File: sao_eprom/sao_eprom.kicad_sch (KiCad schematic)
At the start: 7 parts, among them U1 27C512, U2 24LC32

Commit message: Does more designing ROMulator
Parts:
- removed U1: 27C512, Package_DIP:DIP-28_W15.24mm, symbol Memory_EPROM:27C512
- removed U?: PCAL6416APW, Package_SO:TSSOP-24_4.4x7.8mm_P0.65mm, symbol Interface_Expansion:PCAL6416APW
- removed U? (x2): 74HC273, symbol 74xx:74HC273
- U5: renamed from U2; footprint (none) -> Package_SO:SOIC-8_3.9x4.9mm_P1.27mm
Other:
- added sheet EPROM interface (eprom.kicad_sch)
- note removed: "Address buffer"
- note removed: "EPROM socket"
- note removed: "I/O expander"
- moved on the sheet: JP1, SAO, U5

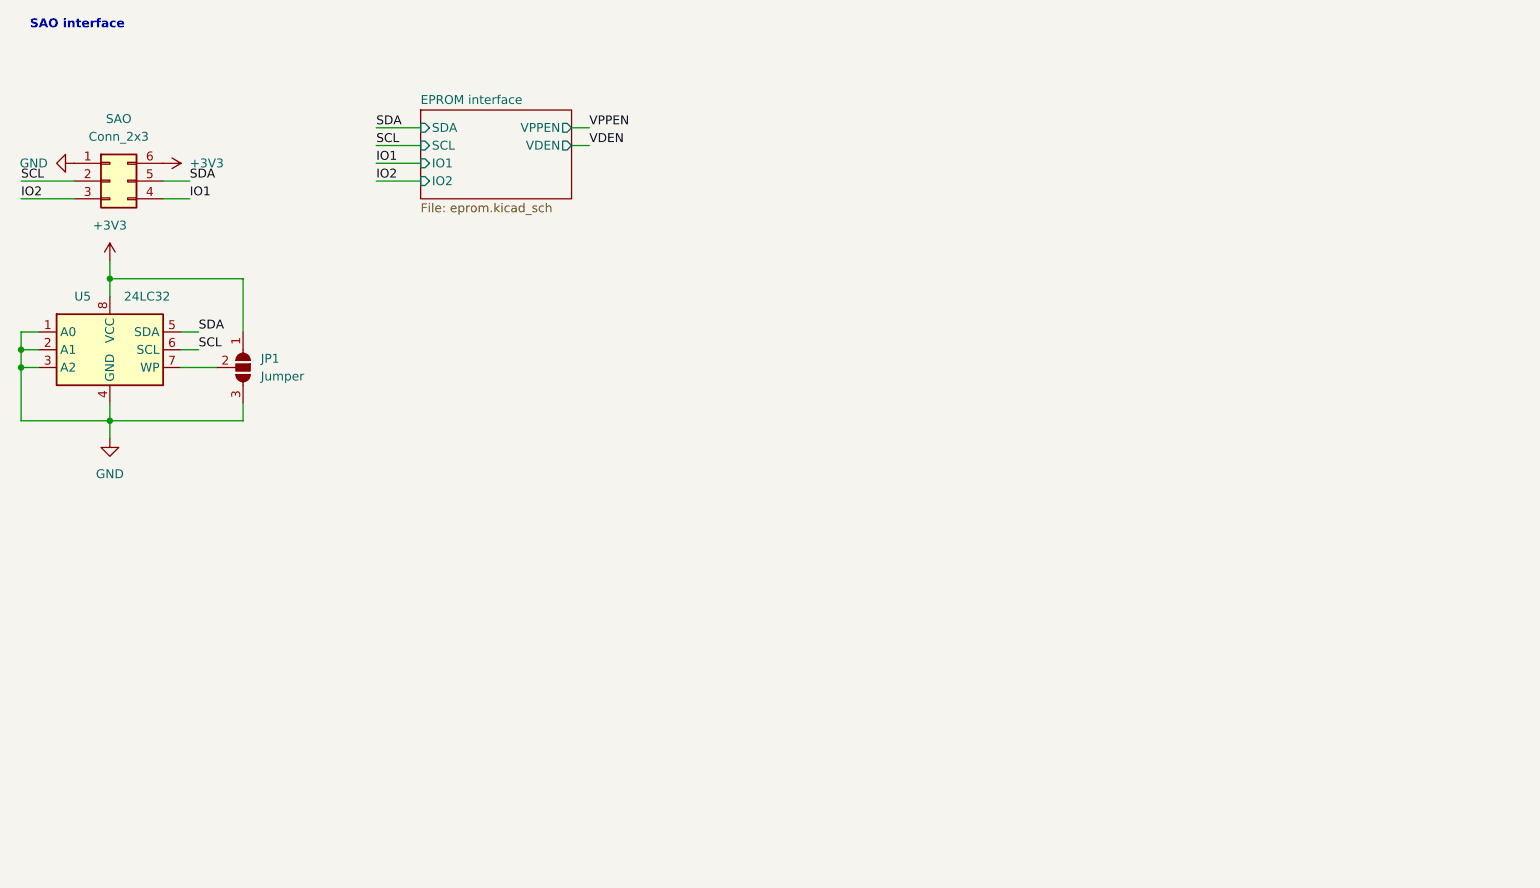
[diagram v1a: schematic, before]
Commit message: Reworks the address circuit
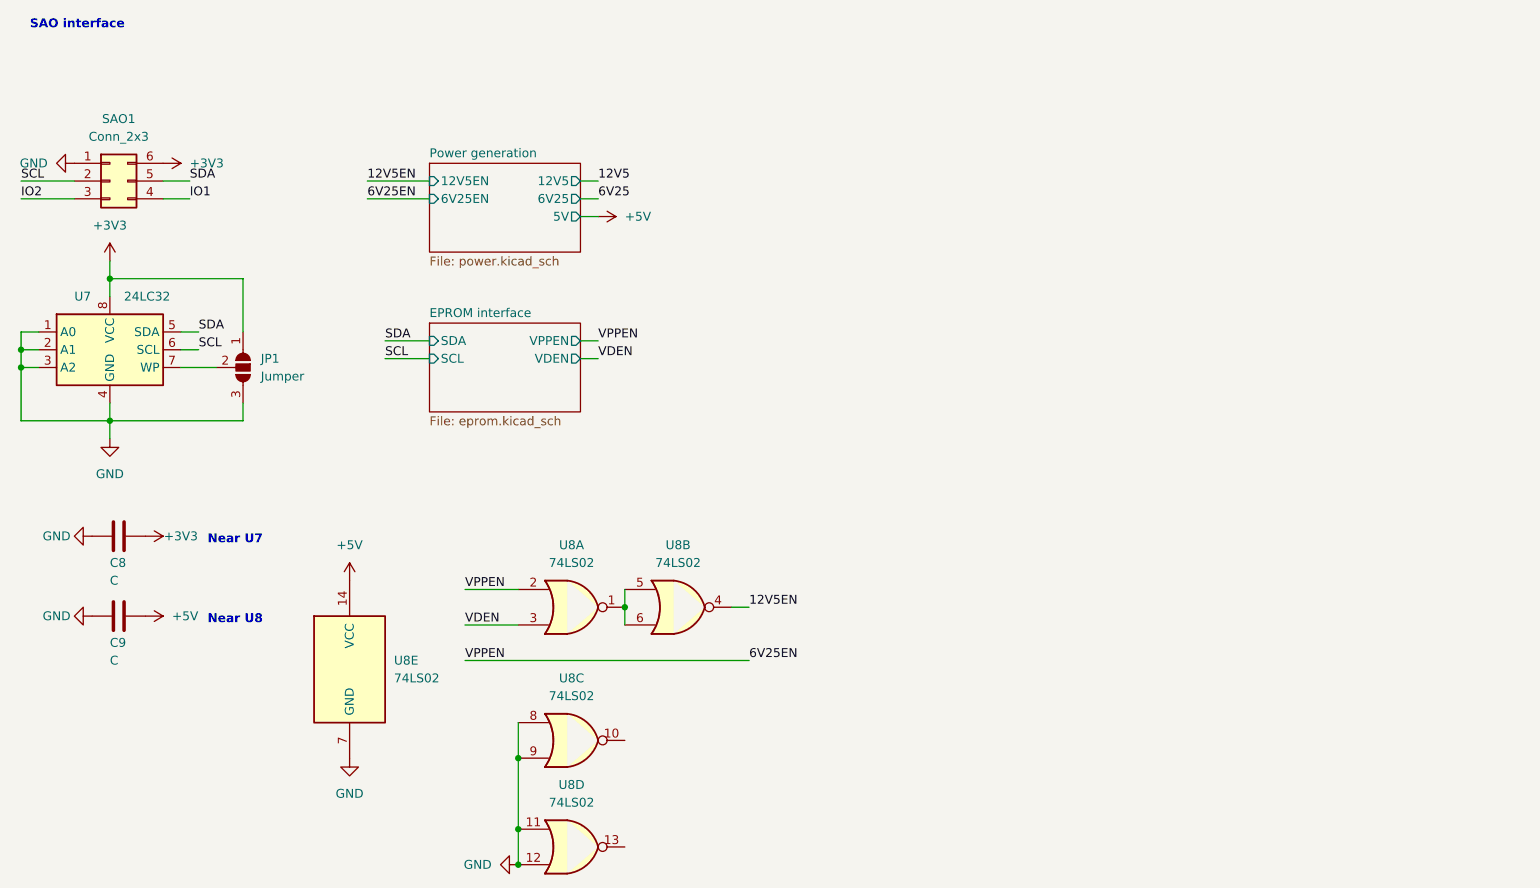
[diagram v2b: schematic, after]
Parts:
- added C8, C9: C, Capacitor_THT:C_Disc_D3.0mm_W1.6mm_P2.50mm, symbol Device:C
- added U8: 74LS02, Package_DIP:DIP-14_W7.62mm, symbol 74xx:74LS02
- JP1: footprint (none) -> Jumper:SolderJumper-3_P1.3mm_Open_RoundedPad1.0x1.5mm_NumberLabels
- SAO1: renamed from SAO; footprint (none) -> Connector_PinHeader_2.54mm:PinHeader_2x03_P2.54mm_Vertical
- renumbered U5 to U7
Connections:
- net +3V3: now also C8.1
- net GND: now also C8.2, C9.2, U8.11, U8.12, U8.7 (GND), U8.8, U8.9
- net VDEN: now also U8.3
- new net: U8.1, U8.5, U8.6
- new net +5V: C9.1, U8.14 (VCC)
- new net 12V5EN: U8.4
- new net 6V25EN: U8.2
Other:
- added sheet Power generation (power.kicad_sch)
- sheet EPROM interface ports: added none; removed IO1, IO2
- note added: "Near U7"
- note added: "Near U8"

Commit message: I know how 2 power now
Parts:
- removed C9: C, Capacitor_THT:C_Disc_D3.0mm_W1.6mm_P2.50mm, symbol Device:C
- removed U8: 74LS02, Package_DIP:DIP-14_W7.62mm, symbol 74xx:74LS02
- added Q1, Q3, Q5: RE1C002UNTCL, Package_TO_SOT_SMD:SOT-416, symbol Transistor_FET:2N7002E
- added Q2, Q4, Q6, Q7: RE1C002ZPTL, Package_TO_SOT_SMD:SOT-416, symbol Transistor_FET:AO3401A
- added R10, R12, R14, R16: 100R, Resistor_THT:R_Axial_DIN0207_L6.3mm_D2.5mm_P7.62mm_Horizontal, symbol Device:R
- added R11, R13, R15: 1K, Resistor_THT:R_Axial_DIN0207_L6.3mm_D2.5mm_P7.62mm_Horizontal, symbol Device:R
- added R17, R18: 10K, Resistor_THT:R_Axial_DIN0207_L6.3mm_D2.5mm_P7.62mm_Horizontal, symbol Device:R
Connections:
- net +5V: now also Q7.2 (S)
- net 12V5: now also Q2.2 (S), Q4.2 (S), R11.1, R13.1
- net 6V25: now also Q6.2 (S), R15.1
- net GND: now also Q1.2 (S), Q3.2 (S), Q5.2 (S), R17.1, R18.2
- net VDEN: now also R12.1, R18.1
- new net: Q1.1 (G), R10.2
- new net: Q1.3 (D), Q2.1 (G), R11.2
- new net: Q5.1 (G), R14.2
- new net: Q5.3 (D), Q6.1 (G), R15.2
- new net: Q7.1 (G), R16.2
- new net: Q3.1 (G), R12.2
- new net: Q3.3 (D), Q4.1 (G), R13.2
- new net VD: Q4.3 (D)
- new net VMEM: Q6.3 (D), Q7.3 (D)
- new net VPP: Q2.3 (D)
- new net VPPEN: R10.1, R14.1, R16.1, R17.2
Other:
- note removed: "Near U8"

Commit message: Finish the first design revision
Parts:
- removed SAO1: Conn_2x3, Connector_PinHeader_2.54mm:PinHeader_2x03_P2.54mm_Vertical, symbol Connector_Generic:Conn_02x03_Counter_Clockwise
- added H1, H2, H3, H4: MountingHole_Pad, symbol Mechanical:MountingHole_Pad
- added J1: Conn_02x03_Odd_Even, Connector_PinHeader_2.54mm:PinHeader_2x03_P2.54mm_Vertical, symbol Connector_Generic:Conn_02x03_Odd_Even
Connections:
- net +3V3: now also J1.2 (Pin_2)
- net GND: now also H1.1, H2.1, H3.1, H4.1, J1.1 (Pin_1)
- net IO1: now also J1.6 (Pin_6)
- net IO2: now also J1.5 (Pin_5)
- net SCL: now also J1.3 (Pin_3)
- net SDA: now also J1.4 (Pin_4)

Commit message: asdafdafa
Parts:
- H1, H2, H3, H4: footprint (none) -> MountingHole:MountingHole_3mm_Pad_Via
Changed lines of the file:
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@@
       (effects (font (size 1.27 1.27)) (justify left))
     )
-    (property "Footprint" "" (id 2) (at 39.37 124.46 0)
+    (property "Footprint" "MountingHole:MountingHole_3mm_Pad_Via" (id 2) (at 39.37 124.46 0)
       (effects (font (size 1.27 1.27)) hide)
     )
@@
       (effects (font (size 1.27 1.27)) (justify left))
     )
-    (property "Footprint" "" (id 2) (at 39.37 119.38 0)
+    (property "Footprint" "MountingHole:MountingHole_3mm_Pad_Via" (id 2) (at 39.37 119.38 0)
       (effects (font (size 1.27 1.27)) hide)
     )
@@
       (effects (font (size 1.27 1.27)) (justify left))
     )
-    (property "Footprint" "" (id 2) (at 39.37 134.62 0)
+    (property "Footprint" "MountingHole:MountingHole_3mm_Pad_Via" (id 2) (at 39.37 134.62 0)
       (effects (font (size 1.27 1.27)) hide)
     )
@@
       (effects (font (size 1.27 1.27)) (justify left))
     )
-    (property "Footprint" "" (id 2) (at 39.37 129.54 0)
+    (property "Footprint" "MountingHole:MountingHole_3mm_Pad_Via" (id 2) (at 39.37 129.54 0)
       (effects (font (size 1.27 1.27)) hide)
     )
@@
     )
     (path "/35ac82b0-ca33-403a-af48-cbfc7e7567dd"
-      (reference "H1") (unit 1) (value "MountingHole_Pad") (footprint "")
+      (reference "H1") (unit 1) (value "MountingHole_Pad") (footprint "MountingHole:MountingHole_3mm_Pad_Via")
     )
     (path "/2d43007f-8bb5-4663-9c50-6fde0d864c8e"
-      (reference "H2") (unit 1) (value "MountingHole_Pad") (footprint "")
+      (reference "H2") (unit 1) (value "MountingHole_Pad") (footprint "MountingHole:MountingHole_3mm_Pad_Via")
     )
     (path "/b311e7ca-786f-4680-83f9-14b49fa76017"
-      (reference "H3") (unit 1) (value "MountingHole_Pad") (footprint "")
+      (reference "H3") (unit 1) (value "MountingHole_Pad") (footprint "MountingHole:MountingHole_3mm_Pad_Via")
     )
     (path "/5f1c73a3-187c-4b01-9943-0cf174dcd226"
-      (reference "H4") (unit 1) (value "MountingHole_Pad") (footprint "")
+      (reference "H4") (unit 1) (value "MountingHole_Pad") (footprint "MountingHole:MountingHole_3mm_Pad_Via")
     )
     (path "/a8e13063-92bd-4cc5-8277-2b18ff1c5b21"

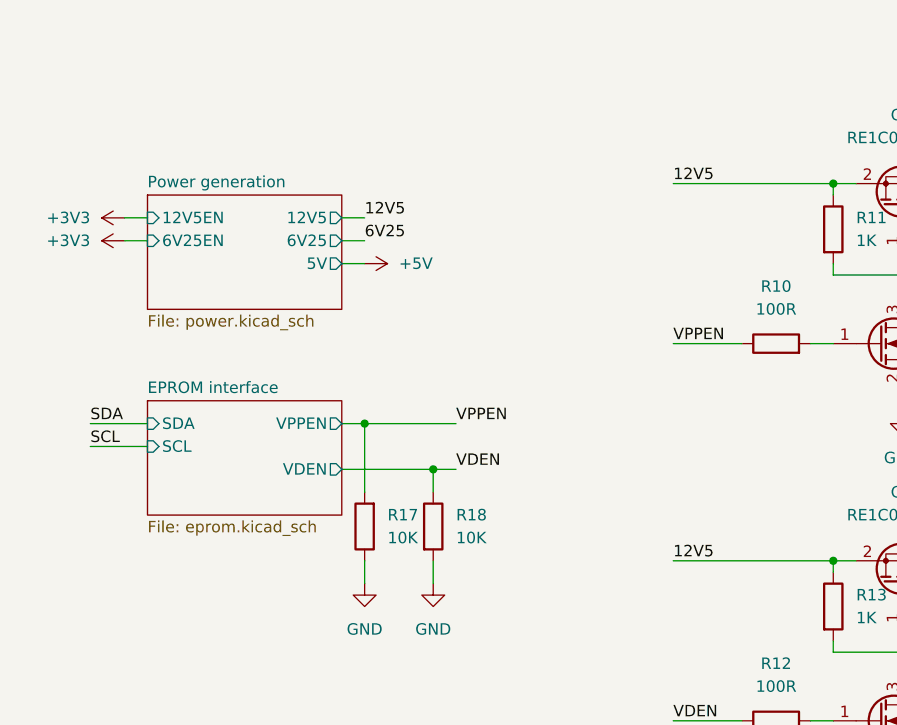
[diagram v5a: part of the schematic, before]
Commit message: Do some resistor calculations
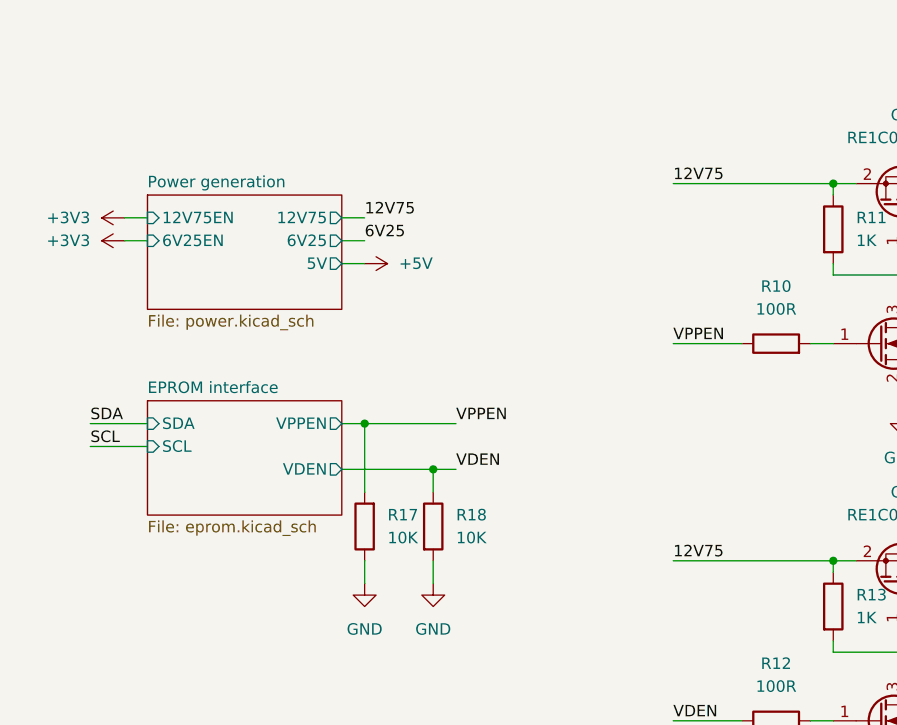
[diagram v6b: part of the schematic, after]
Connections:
- net 12V5 renamed 12V75
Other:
- sheet Power generation ports: added 12V75, 12V75EN; removed 12V5, 12V5EN
- title: (none) -> Main sheet
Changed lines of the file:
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@@
 (kicad_sch (version 20211123) (generator eeschema)
   (paper "A4")
+  (title_block
+    (title "Main sheet")
+  )
   (junction (at 219.71 60.96) (diameter 0) (color 0 0 0 0)
   )
@@
     (effects (font (size 1.27 1.27)) (justify left bottom))
   )
+  (label "12V75" (at 144.78 50.8 0)
+    (effects (font (size 1.27 1.27)) (justify left bottom))
+  )
   (label "SDA" (at 53.34 76.2 0)
     (effects (font (size 1.27 1.27)) (justify left bottom))
@@
     (effects (font (size 1.27 1.27)) (justify left bottom))
   )
-  (label "12V5" (at 110.49 54.61 0)
+  (label "12V75" (at 110.49 54.61 0)
     (effects (font (size 1.27 1.27)) (justify left bottom))
   )
@@
     (effects (font (size 1.27 1.27)) (justify left bottom))
   )
+  (label "12V75" (at 144.78 92.71 0)
+    (effects (font (size 1.27 1.27)) (justify left bottom))
+  )
   (label "VPPEN" (at 120.65 77.47 0)
     (effects (font (size 1.27 1.27)) (justify left bottom))
   )
-  (label "12V5" (at 144.78 50.8 0)
-    (effects (font (size 1.27 1.27)) (justify left bottom))
-  )
   (label "SDA" (at 80.01 77.47 0)
     (effects (font (size 1.27 1.27)) (justify left bottom))
@@
   )
   (label "6V25" (at 194.31 50.8 0)
-    (effects (font (size 1.27 1.27)) (justify left bottom))
-  )
-  (label "12V5" (at 144.78 92.71 0)
     (effects (font (size 1.27 1.27)) (justify left bottom))
   )
@@
       (effects (font (size 1.27 1.27)) (justify left))
     )
-    (pin "12V5EN" input (at 86.36 54.61 180)
-      (effects (font (size 1.27 1.27)) (justify left))
-    )
-    (pin "12V5" output (at 107.95 54.61 0)
+    (pin "12V75EN" input (at 86.36 54.61 180)
+      (effects (font (size 1.27 1.27)) (justify left))
+    )
+    (pin "12V75" output (at 107.95 54.61 0)
       (effects (font (size 1.27 1.27)) (justify right))
     )
@@
     )
     (path "/04a0465a-e9b3-4bee-95e7-0c6308f8d13f/c0bf6ce3-056a-4835-ac9d-29e3dfe8f919"
-      (reference "R6") (unit 1) (value "R") (footprint "Resistor_THT:R_Axial_DIN0207_L6.3mm_D2.5mm_P7.62mm_Horizontal")
+      (reference "R6") (unit 1) (value "1K") (footprint "Resistor_THT:R_Axial_DIN0207_L6.3mm_D2.5mm_P7.62mm_Horizontal")
     )
     (path "/04a0465a-e9b3-4bee-95e7-0c6308f8d13f/067c629d-b7a1-4db3-9d5d-9a57ac384e50"
-      (reference "R7") (unit 1) (value "R") (footprint "Resistor_THT:R_Axial_DIN0207_L6.3mm_D2.5mm_P7.62mm_Horizontal")
+      (reference "R7") (unit 1) (value "250R") (footprint "Resistor_THT:R_Axial_DIN0207_L6.3mm_D2.5mm_P7.62mm_Horizontal")
     )
     (path "/04a0465a-e9b3-4bee-95e7-0c6308f8d13f/523757fc-686f-46ad-a427-0f51abcdf1ff"
-      (reference "R8") (unit 1) (value "R") (footprint "Resistor_THT:R_Axial_DIN0207_L6.3mm_D2.5mm_P7.62mm_Horizontal")
+      (reference "R8") (unit 1) (value "1K") (footprint "Resistor_THT:R_Axial_DIN0207_L6.3mm_D2.5mm_P7.62mm_Horizontal")
     )
     (path "/04a0465a-e9b3-4bee-95e7-0c6308f8d13f/24fd4f39-ced7-4c95-87af-53065b89e608"
-      (reference "R9") (unit 1) (value "R") (footprint "Resistor_THT:R_Axial_DIN0207_L6.3mm_D2.5mm_P7.62mm_Horizontal")
+      (reference "R9") (unit 1) (value "330R") (footprint "Resistor_THT:R_Axial_DIN0207_L6.3mm_D2.5mm_P7.62mm_Horizontal")
     )
     (path "/738c1106-814d-43bc-b2fc-80b974ad345e"
